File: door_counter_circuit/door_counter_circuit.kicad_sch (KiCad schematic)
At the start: 12 parts

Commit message: circuit board drafted
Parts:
- removed U?: TSDP341xx, OptoDevice:Vishay_MOLD-3Pin, symbol Interface_Optical:TSDP341xx
- removed U?: RTC_module, symbol modules:RTC_module
- removed U?: SD_Card_Module, symbol modules:SD_Card_Module
- added BT1: BS-7, bs-7:BAT_BS-7, symbol bs-7:BS-7
- added C1, C2, C3, C4, C5, C6, C7: 0.1uF, Capacitor_SMD:C_0402_1005Metric, symbol Device:C
- added H1, H2, H3, H4: MountingHole_Pad, MountingHole:MountingHole_5mm_Pad_Via, symbol Mechanical:MountingHole_Pad
- added J1, J2: Conn_01x20_Male, Connector_PinHeader_2.54mm:PinHeader_1x20_P2.54mm_Vertical, symbol Connector:Conn_01x20_Male
- added J3: Prototype_Space, Library:Prototype Space, symbol Library:Prototype_Space
- added JP1: Jumper_3_Open, Connector_PinHeader_2.54mm:PinHeader_1x03_P2.54mm_Vertical, symbol Jumper:Jumper_3_Open
- added MICRO_SD1: TF-01A, tf01a:TF-01A, symbol tf01a:TF-01A
- added R1, R2, R3, R4, R5: 10k, Resistor_SMD:R_0603_1608Metric, symbol Device:R
- added SW1, SW3: SW_Push, Button_Switch_THT:SW_PUSH_6mm_H4.3mm, symbol Switch:SW_Push
- added U3: TSDP341xx, OptoDevice:Vishay_MOLD-3Pin, symbol Interface_Optical:TSDP341xx
- added U5: DS1302+, Package_DIP:DIP-8_W7.62mm, symbol Timer_RTC:DS1302+
- added Y1: 32.768kHz, Crystal:Crystal_C26-LF_D2.1mm_L6.5mm_Horizontal, symbol Device:Crystal
- D1: renamed from D?; footprint (none) -> LED_THT:LED_D3.0mm_Horizontal_O1.27mm_Z6.0mm
- R6, R7: renamed from R?; footprint (none) -> Resistor_SMD:R_0603_1608Metric
- RV1: renamed from RV?; footprint (none) -> Potentiometer_THT:Potentiometer_Bourns_3296W_Vertical
- SW2: renamed from SW?; footprint (none) -> Rotary_Encoder:RotaryEncoder_Alps_EC11E-Switch_Vertical_H20mm
- U1: renamed from U?; symbol RPi_Pico:Pico -> modules:Pico
- U4: renamed from U?; footprint (none) -> ssd1306:SSD1306
- gave numbers to parts that had none: 2
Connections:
- net +3V3: now also U4.2 (VCC), C1.1, C3.1, C4.1, C5.2, C6.1, J2.16 (Pin_16), J3.10A, J3.11A, J3.12A, J3.13A, J3.14A, J3.15A, J3.16A, J3.1A, J3.2A, J3.3A, J3.4A, J3.5A, J3.6A, J3.7A, J3.8A, J3.9A, JP1.2 (C), MICRO_SD1.4 (VDD), R1.1, R2.1, R3.1, R4.1, R5.1, U3.3 (Vs), U5.1 (VCC2)
- net +5V: now also C2.1, J2.20 (Pin_20), J3.10R, J3.11R, J3.12R, J3.13R, J3.14R, J3.15R, J3.16R, J3.1R, J3.2R, J3.3R, J3.4R, J3.5R, J3.6R, J3.7R, J3.8R, J3.9R
- net GND: now also SW2.C, SW2.S1, U1.42 (GND), U4.1 (GND), BT1.-, C1.2, C2.2, C3.2, C4.2, C5.1, C6.2, C7.2, H1.1, H2.1, H3.1, H4.1, J1.13 (Pin_13), J1.18 (Pin_18), J1.3 (Pin_3), J1.8 (Pin_8), J2.18 (Pin_18), J2.3 (Pin_3), J2.8 (Pin_8), J3.10B, J3.10T, J3.11B, J3.11T, J3.12B, J3.12T, J3.13B, J3.13T, J3.14B, J3.14T, J3.15B, J3.15T, J3.16B, J3.16T, J3.1B, J3.1T, J3.2B, J3.2T, J3.3B, J3.3T, J3.4B, J3.4T, J3.5B, J3.5T, J3.6B, J3.6T, J3.7B, J3.7T, J3.8B, J3.8T, J3.9B, J3.9T, MICRO_SD1.6 (VSS), MICRO_SD1.MP1 (SHIELD), MICRO_SD1.MP2 (SHIELD), MICRO_SD1.MP3 (SHIELD), MICRO_SD1.MP4 (SHIELD), SW1.2, SW3.2, U3.2 (GND), U5.4 (GND)
- net at R6.1, RV1.2: now also RV1.3
- net at SW2.A: now also U1.10 (GPIO7), J1.10 (Pin_10)
- net at SW2.B: now also U1.9 (GPIO6), J1.9 (Pin_9)
- net at SW2.S2: now also U1.7 (GPIO5), J1.7 (Pin_7)
- net SD_MISO: now reaches U1.1 (GPIO0)
- net SD_MISO: now also J1.1 (Pin_1), MICRO_SD1.7 (DAT0), R4.2
- net OLED_SDA: now reaches U1.11 (GPIO8)
- net OLED_SDA: now also U4.4 (SDA), J1.11 (Pin_11)
- net OLED_SCL: now reaches U1.12 (GPIO9)
- net OLED_SCL: now also U4.3 (SCL), J1.12 (Pin_12)
- net RTC_DAT: now reaches U1.14 (GPIO10)
- net RTC_DAT: now also J1.14 (Pin_14), U5.6 (I/O)
- net RTC_RST: now reaches U1.15 (GPIO11)
- net RTC_RST: now also J1.15 (Pin_15), U5.5 (CE)
- net RTC_CLK: now reaches U1.16 (GPIO12)
- net RTC_CLK: now also J1.16 (Pin_16), U5.7 (SCLK)
- net IR_CONTROL: now reaches U1.17 (GPIO13)
- net IR_CONTROL: now also R7.1, J1.17 (Pin_17)
- net IR_DETECT_1: now reaches U1.19 (GPIO14)
- net IR_DETECT_1: now also U2.1 (OUT), J1.19 (Pin_19)
- net SD_CS: now reaches U1.2 (GPIO1)
- net SD_CS: now also J1.2 (Pin_2), MICRO_SD1.2 (CD/DAT3), R1.2
- net IR_DETECT_2: now reaches U1.20 (GPIO15)
- net IR_DETECT_2: now also J1.20 (Pin_20), U3.1 (OUT)
- net C1: now reaches U1.21 (GPIO16)
- net C1: now also J2.1 (Pin_1), J3.1C, J3.1D, J3.1E
- net C2: now reaches U1.22 (GPIO17)
- net C2: now also J2.2 (Pin_2), J3.2C, J3.2D, J3.2E
- net C3: now reaches U1.24 (GPIO18)
- net C3: now also J2.4 (Pin_4), J3.3C, J3.3D, J3.3E
- net C4: now reaches U1.25 (GPIO19)
- net C4: now also J2.5 (Pin_5), J3.4C, J3.4D, J3.4E
- net C5: now reaches U1.26 (GPIO20)
- net C5: now also J2.6 (Pin_6), J3.5C, J3.5D, J3.5E
- net C6: now reaches U1.27 (GPIO21)
- net C6: now also J2.7 (Pin_7), J3.6C, J3.6D, J3.6E
- net M13: now reaches U1.29 (GPIO22)
- net M13: now also J2.9 (Pin_9), J3.13M, J3.13N, J3.13P
- net at U1.30 (RUN): now also J2.10 (Pin_10), SW3.1
- net M14: now reaches U1.31 (GPIO26_ADC0)
- net M14: now also J2.11 (Pin_11), J3.14M, J3.14N, J3.14P
- net M15: now reaches U1.32 (GPIO27_ADC1)
- net M15: now also J2.12 (Pin_12), J3.15M, J3.15N, J3.15P
- net at U1.33 (AGND): now also J2.13 (Pin_13)
- net M16: now reaches U1.34 (GPIO28_ADC2)
- net M16: now also J2.14 (Pin_14), J3.16M, J3.16N, J3.16P
- net at U1.35 (ADC_VREF): now also J2.15 (Pin_15)
- net at U1.37 (3V3_EN): now also J2.17 (Pin_17), SW1.1
- net at U1.39 (VSYS): now also J2.19 (Pin_19)
- net SD_SCK: now reaches U1.4 (GPIO2)
- net SD_SCK: now also J1.4 (Pin_4), MICRO_SD1.5 (CLK)
- net SD_MOSI: now reaches U1.5 (GPIO3)
- net SD_MOSI: now also J1.5 (Pin_5), MICRO_SD1.8 (DAT1), R3.2
- net SD_DET: now reaches U1.6 (GPIO4)
- net SD_DET: now also J1.6 (Pin_6), MICRO_SD1.CD1 (CD)
- new net: BT1.+, C7.1, JP1.3 (B), U5.8 (VCC1)
- new net: U5.3 (X2), Y1.1
- new net: U5.2 (X1), Y1.2
- new net: MICRO_SD1.1 (DAT2), R2.2
- new net: MICRO_SD1.3 (CMD), R5.2
- new net: J3.10C, J3.10D, J3.10E
- new net: J3.10F, J3.10G, J3.10H
- new net: J3.10J, J3.10K, J3.10L
- new net: J3.10M, J3.10N, J3.10P
- new net: J3.11C, J3.11D, J3.11E
- new net: J3.11F, J3.11G, J3.11H
- new net: J3.11J, J3.11K, J3.11L
- new net: J3.11M, J3.11N, J3.11P
- new net: J3.12C, J3.12D, J3.12E
- new net: J3.12F, J3.12G, J3.12H
- new net: J3.12J, J3.12K, J3.12L
- new net: J3.12M, J3.12N, J3.12P
- new net: J3.13C, J3.13D, J3.13E
- new net: J3.13F, J3.13G, J3.13H
- new net: J3.13J, J3.13K, J3.13L
- new net: J3.14C, J3.14D, J3.14E
- new net: J3.14F, J3.14G, J3.14H
- new net: J3.14J, J3.14K, J3.14L
- new net: J3.15C, J3.15D, J3.15E
- new net: J3.15F, J3.15G, J3.15H
- new net: J3.15J, J3.15K, J3.15L
- new net: J3.16C, J3.16D, J3.16E
- new net: J3.16F, J3.16G, J3.16H
- new net: J3.16J, J3.16K, J3.16L
- new net: J3.1F, J3.1G, J3.1H
- new net: J3.1J, J3.1K, J3.1L
- new net: J3.1M, J3.1N, J3.1P
- new net: J3.2F, J3.2G, J3.2H
- new net: J3.2J, J3.2K, J3.2L
- new net: J3.2M, J3.2N, J3.2P
- new net: J3.3F, J3.3G, J3.3H
- new net: J3.3J, J3.3K, J3.3L
- new net: J3.3M, J3.3N, J3.3P
- new net: J3.4F, J3.4G, J3.4H
- new net: J3.4J, J3.4K, J3.4L
- new net: J3.4M, J3.4N, J3.4P
- new net: J3.5F, J3.5G, J3.5H
- new net: J3.5J, J3.5K, J3.5L
- new net: J3.5M, J3.5N, J3.5P
- new net: J3.6F, J3.6G, J3.6H
- new net: J3.6J, J3.6K, J3.6L
- new net: J3.6M, J3.6N, J3.6P
- new net: J3.7C, J3.7D, J3.7E
- new net: J3.7F, J3.7G, J3.7H
- new net: J3.7J, J3.7K, J3.7L
- new net: J3.7M, J3.7N, J3.7P
- new net: J3.8C, J3.8D, J3.8E
- new net: J3.8F, J3.8G, J3.8H
- new net: J3.8J, J3.8K, J3.8L
- new net: J3.8M, J3.8N, J3.8P
- new net: J3.9C, J3.9D, J3.9E
- new net: J3.9F, J3.9G, J3.9H
- new net: J3.9J, J3.9K, J3.9L
- new net: J3.9M, J3.9N, J3.9P
- no-connect marks 0 -> 3
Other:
- moved on the sheet: D1, Q1, R6, R7, RV1, SW2, U1, U2, U4

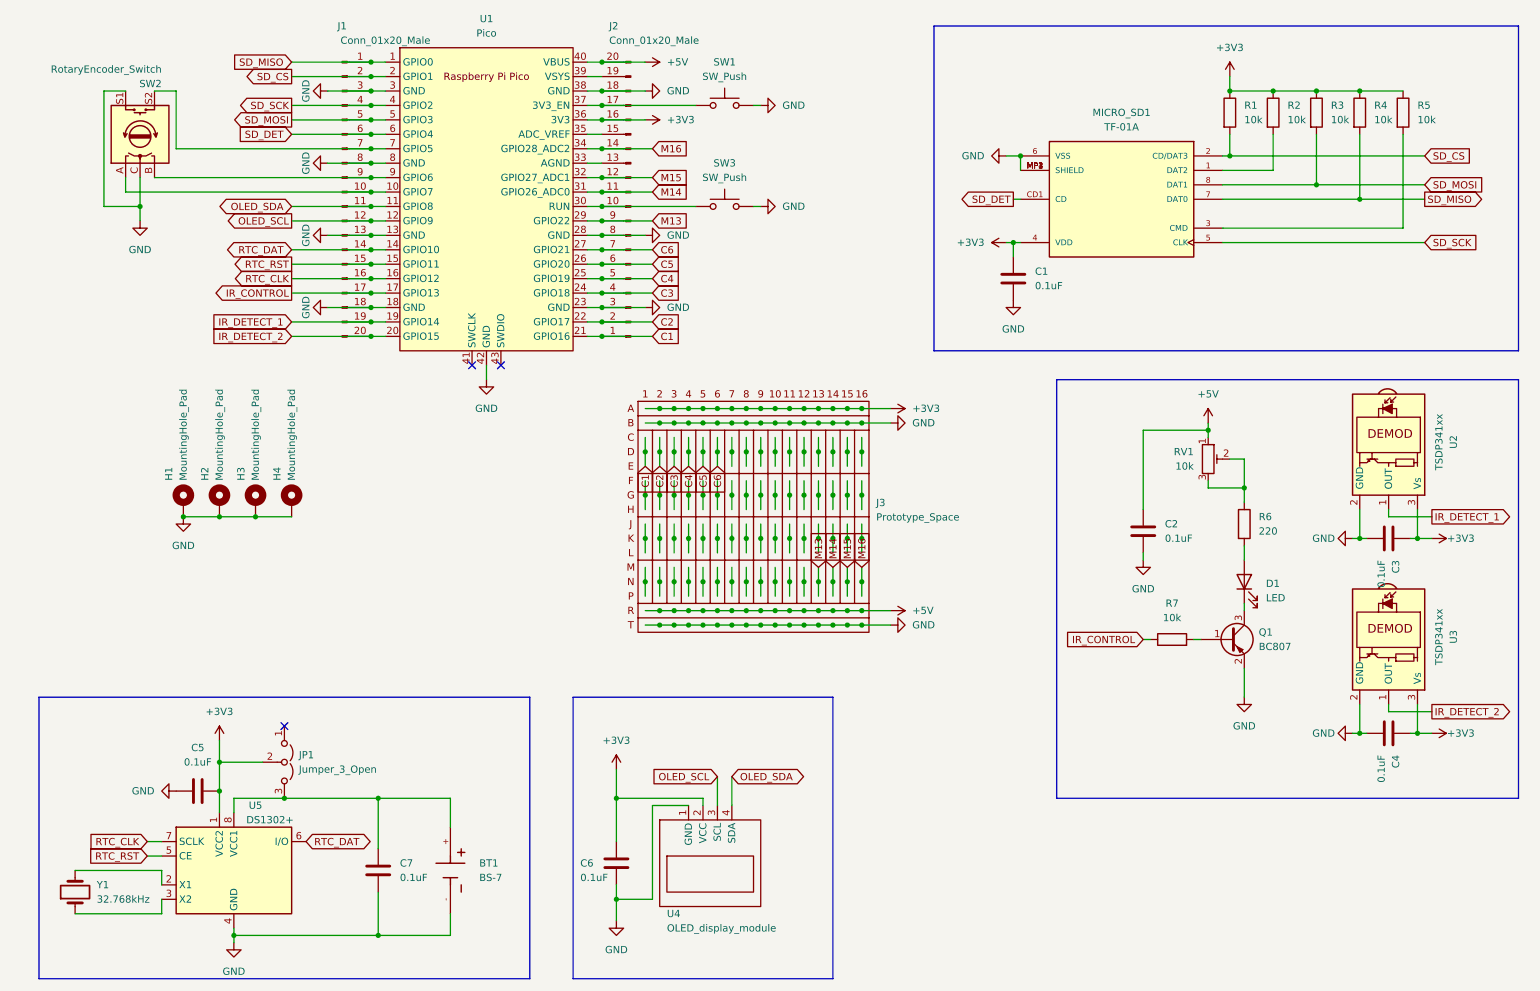
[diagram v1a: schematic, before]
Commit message: include a configurable transistor footprint
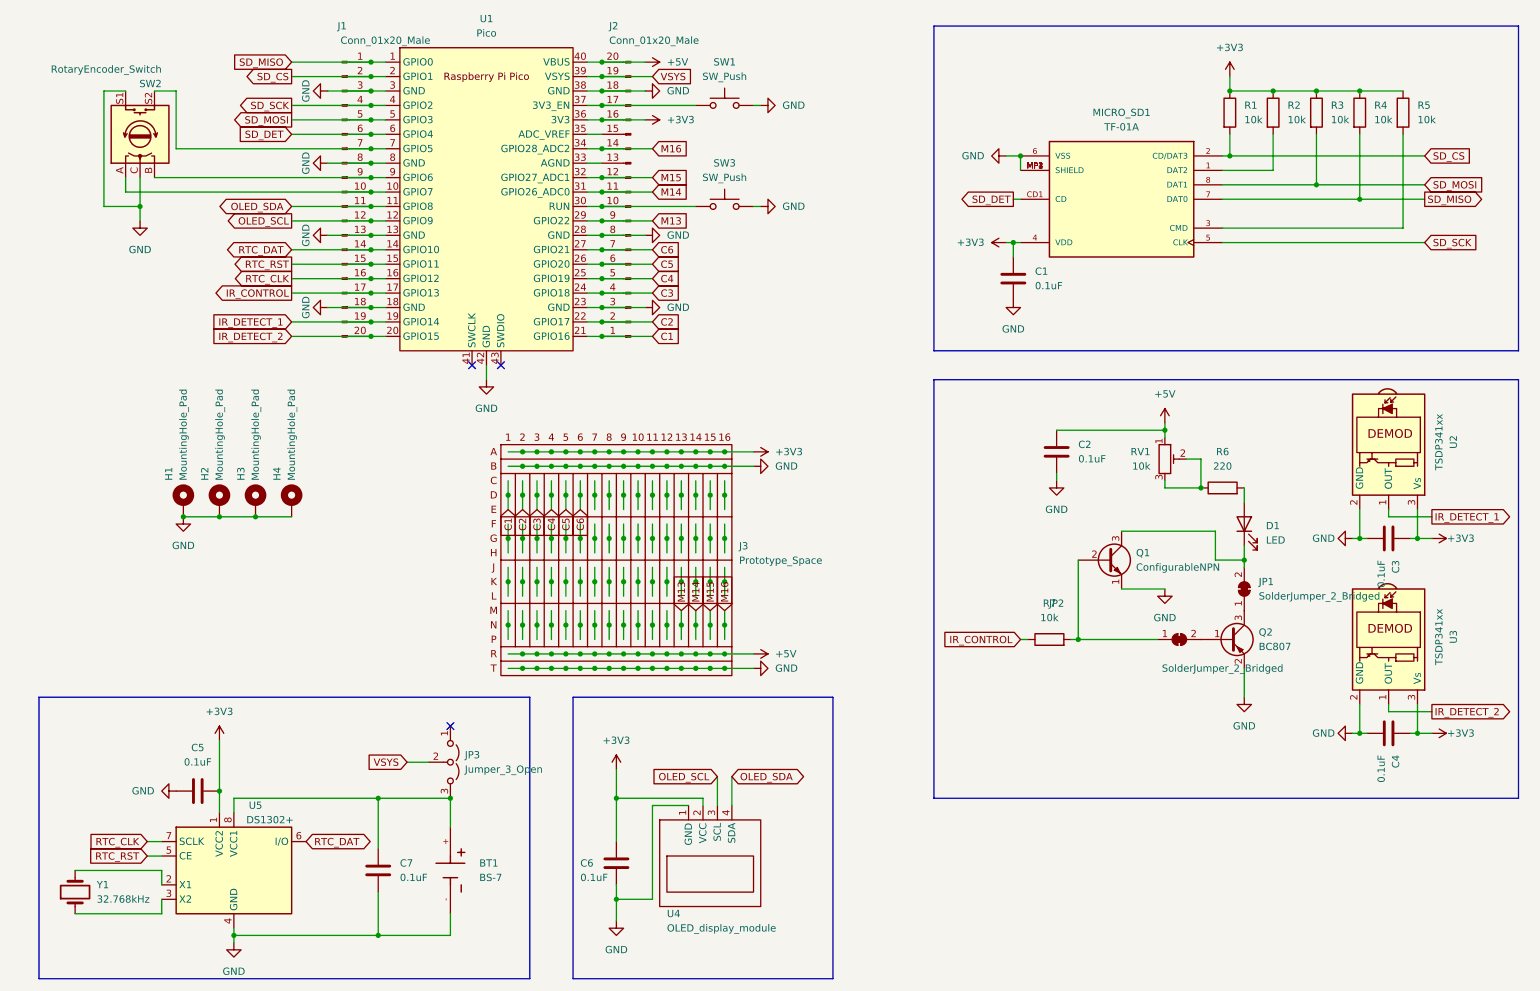
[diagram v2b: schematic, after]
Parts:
- added JP1, JP2: SolderJumper_2_Bridged, Jumper:SolderJumper-2_P1.3mm_Bridged_RoundedPad1.0x1.5mm, symbol Jumper:SolderJumper_2_Bridged
- added Q1: ConfigurableNPN, Library:TO-92-configurable, symbol Library:ConfigurableNPN
- H1, H2, H3, H4: footprint MountingHole:MountingHole_5mm_Pad_Via -> MountingHole:MountingHole_2.5mm_Pad_Via
- renumbered JP1 to JP3, Q1 to Q2
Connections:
- net +3V3: no longer JP3.2 (C)
- net GND: now also Q1.1 (E), Q1.4 (emitter_duplicate)
- net VSYS: now reaches J2.19 (Pin_19), U1.39 (VSYS)
- net VSYS: now also JP3.2 (C)
- net at D1.1 (K): now also JP1.2 (B), Q1.3 (C), Q1.5 (collector_duplicate); no longer Q2.3 (C)
- net at R7.2: now also JP2.1 (A), Q1.2 (B); no longer Q2.1 (B)
- new net: JP2.2 (B), Q2.1 (B)
- new net: JP1.1 (A), Q2.3 (C)
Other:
- moved on the sheet: C2, D1, J3, JP3, R6, R7, RV1

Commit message: manufacturing outputs
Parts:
- added FID1, FID2, FID3, FID4: Fiducial, Fiducial:Fiducial_1mm_Mask2mm, symbol Mechanical:Fiducial
- added TP1, TP2, TP3: TestPoint, TestPoint:TestPoint_Pad_4.0x4.0mm, symbol Connector:TestPoint
- BT1, D1, H1, H2, H3, H4, J1, J2, J3, JP2, RV1, SW3, U1, Y1: now left out of the parts list
- C1: LCSC (none) -> C1525
- C2: renamed from C7; LCSC (none) -> C1525
- C3: renamed from C6; LCSC (none) -> C1525
- C4: renamed from C5; LCSC (none) -> C1525
- C5: renamed from C2; LCSC (none) -> C1525
- C6: renamed from C3; LCSC (none) -> C1525
- C7: renamed from C4; LCSC (none) -> C1525
- JP1: renamed from JP3; now left out of the parts list
- JP3: renamed from JP1; now left out of the parts list
- MICRO_SD1: LCSC (none) -> C91145
- Q1: renamed from Q2; value BC807 -> MMS9013-H-TP; LCSC (none) -> C90160
- Q2: renamed from Q1; now left out of the parts list
- R1: renamed from R2; LCSC (none) -> C25804
- R2: renamed from R1; LCSC (none) -> C25804
- R3: renamed from R5; LCSC (none) -> C25804
- R4: LCSC (none) -> C25804
- R5: renamed from R3; LCSC (none) -> C25804
- R6: renamed from R7; LCSC (none) -> C25804
- R7: renamed from R6; footprint Resistor_SMD:R_0603_1608Metric -> Resistor_SMD:R_0805_2012Metric; LCSC (none) -> C17557
- SW1: renamed from SW2; now left out of the parts list
- SW2: renamed from SW1; now left out of the parts list
- U2: renamed from U4; now left out of the parts list
- U3: renamed from U5; now left out of the parts list
- U4: renamed from U2; now left out of the parts list
- U5: renamed from U3; now left out of the parts list
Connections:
- net GND: now also TP1.1, TP2.1, TP3.1

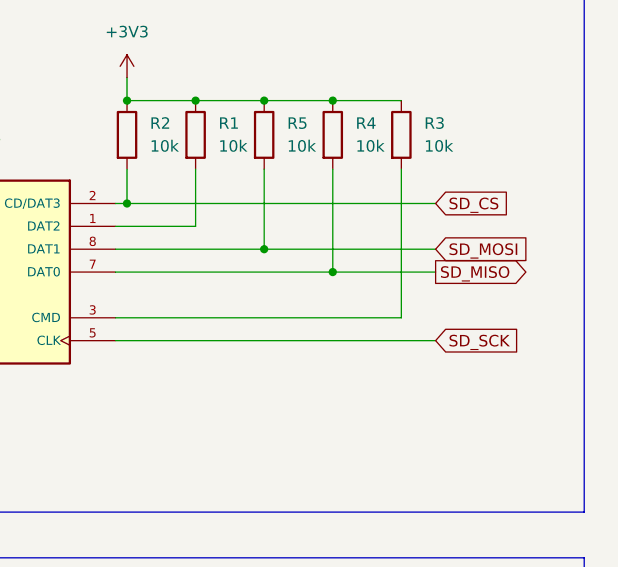
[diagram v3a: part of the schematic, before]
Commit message: fix to SD circuit
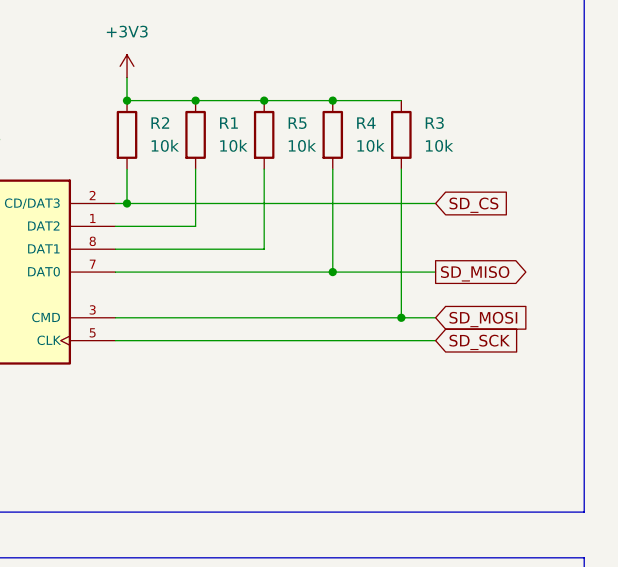
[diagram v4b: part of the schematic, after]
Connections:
- net SD_MOSI: now also MICRO_SD1.3 (CMD), R3.2; no longer MICRO_SD1.8 (DAT1), R5.2
- new net: MICRO_SD1.8 (DAT1), R5.2
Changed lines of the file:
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@@
   (junction (at 120.65 130.81) (diameter 0) (color 0 0 0 0)
   )
+  (junction (at 257.81 60.96) (diameter 0) (color 0 0 0 0)
+  )
   (junction (at 130.81 138.43) (diameter 0) (color 0 0 0 0)
   )
@@
   )
   (junction (at 76.2 110.49) (diameter 0) (color 0 0 0 0)
-  )
-  (junction (at 242.57 53.34) (diameter 0) (color 0 0 0 0)
   )
   (junction (at 49.53 160.02) (diameter 0) (color 0 0 0 0)
@@
     (stroke (width 0) (type default) (color 0 0 0 0))
   )
+  (wire (pts (xy 257.81 60.96) (xy 261.62 60.96))
+    (stroke (width 0) (type default) (color 0 0 0 0))
+  )
   (wire (pts (xy 120.65 135.89) (xy 123.19 135.89))
     (stroke (width 0) (type default) (color 0 0 0 0))
@@
   )
   (wire (pts (xy 52.07 161.29) (xy 52.07 163.83))
-    (stroke (width 0) (type default) (color 0 0 0 0))
-  )
-  (wire (pts (xy 242.57 53.34) (xy 261.62 53.34))
     (stroke (width 0) (type default) (color 0 0 0 0))
   )
@@
     )
   )
-  (global_label "SD_MOSI" (shape input) (at 261.62 53.34 0) (fields_autoplaced)
+  (global_label "SD_MOSI" (shape input) (at 261.62 60.96 0) (fields_autoplaced)
     (effects (font (size 1.27 1.27)) (justify left))
-    (property "Intersheet References" "${INTERSHEET_REFS}" (id 0) (at 272.0764 53.2606 0)
+    (property "Intersheet References" "${INTERSHEET_REFS}" (id 0) (at 272.0764 60.8806 0)
       (effects (font (size 1.27 1.27)) (justify left) hide)
     )
